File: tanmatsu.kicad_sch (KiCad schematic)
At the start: 41 parts, among them J1 USB device, J10 Expansion I3C, J12 SAO, J2 USB host, J4 Headphone, J5 External Add-On (SAO / PMOD), J6 Internal Add-On, J7 Speaker, J8 Micro_SD_Card, J9 CAMERA, SW3 Boot, U28 USBLC6-2P6, U29 USBLC6-2P6, U30 ESD, U31 ESD, U4 CH334R, Y1 12MHz

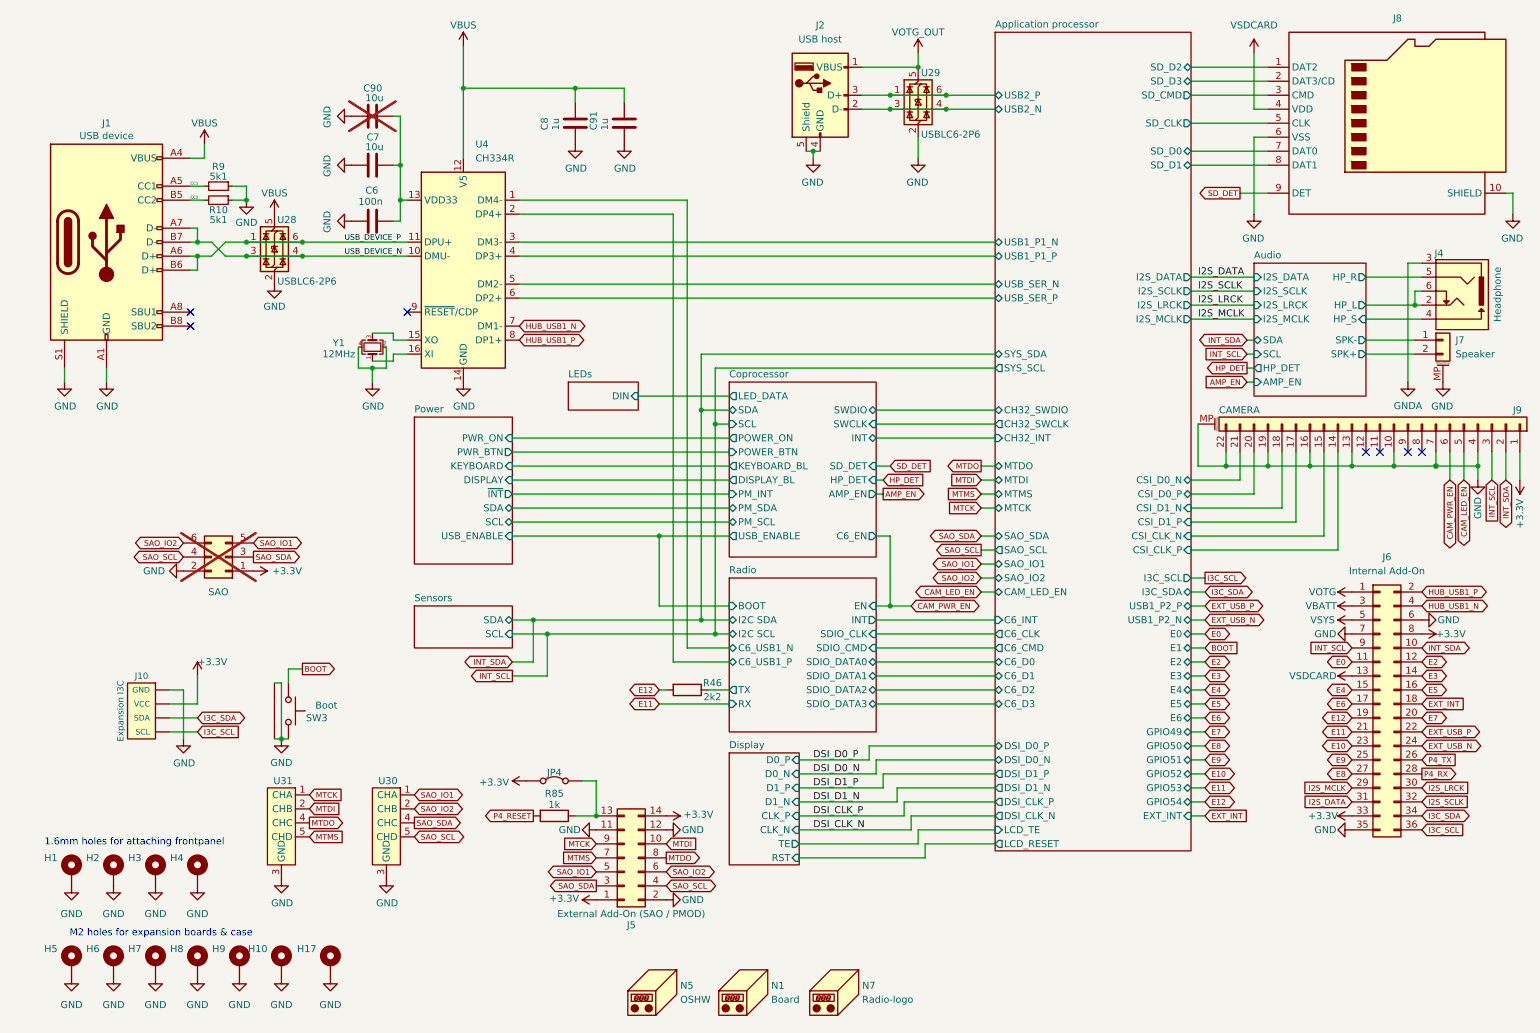
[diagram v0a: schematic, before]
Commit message: Add level shifter for VSDCARD GPIOs, remove USB to serial chip
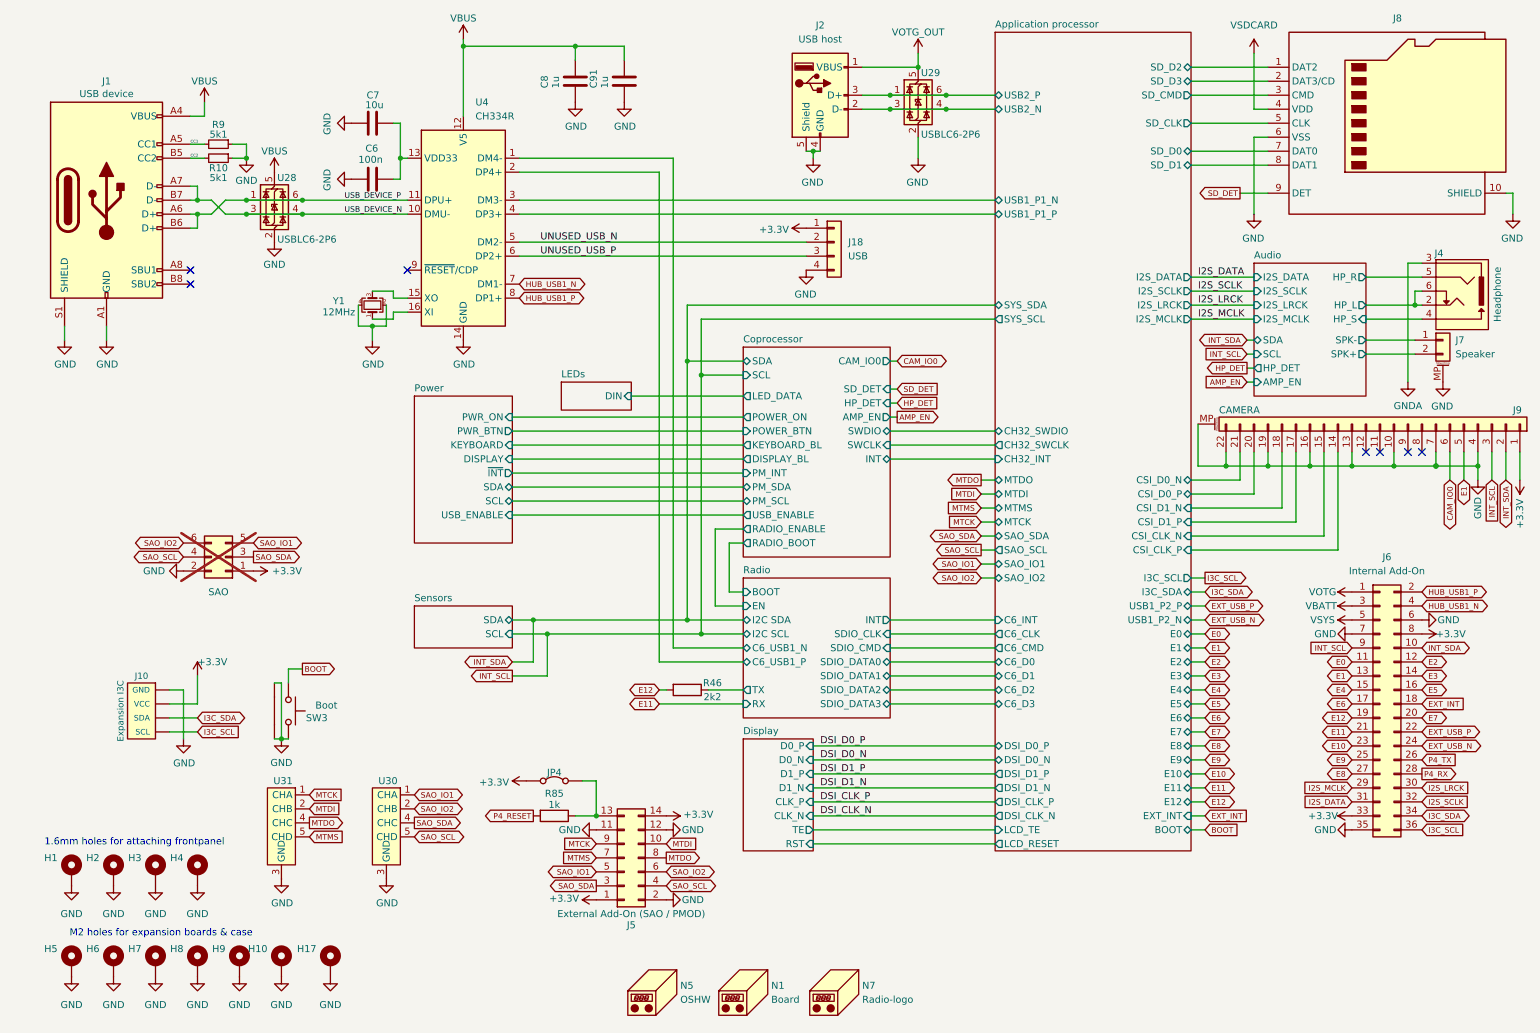
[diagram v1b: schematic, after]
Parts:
- removed C90: 10u, Capacitor_SMD:C_0805_2012Metric, symbol Device:C
- added J18: USB, Connector_PinHeader_2.54mm:PinHeader_1x04_P2.54mm_Vertical_SMD_Pin1Left, symbol Connector_Generic:Conn_01x04
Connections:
- net +3.3V: now also J18.1 (Pin_1)
- net GND: now also J18.4 (Pin_4)
- net VSDCARD: no longer J6.13 (Pin_13)
- net Application processor/USB_SER_N renamed UNUSED_USB_N
- net UNUSED_USB_N: now also J18.2 (Pin_2)
- net Application processor/USB_SER_P renamed UNUSED_USB_P
- net UNUSED_USB_P: now also J18.3 (Pin_3)
- net CAM_LED_EN renamed E1
- net E1: now also J6.13 (Pin_13)
- net CAM_PWR_EN renamed CAM_IO0
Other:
- sheet Application processor ports: added BOOT, E10, E11, E12, E7, E8, E9; removed CAM_LED_EN, GPIO49, GPIO50, GPIO51, GPIO52, GPIO53, GPIO54, USB_SER_N, USB_SER_P
- sheet Coprocessor ports: added CAM_IO0, RADIO_BOOT, RADIO_ENABLE; removed C6_EN
- moved on the sheet: C6, C7, C8, C91, J1, R10, R9, U28, U4, Y1

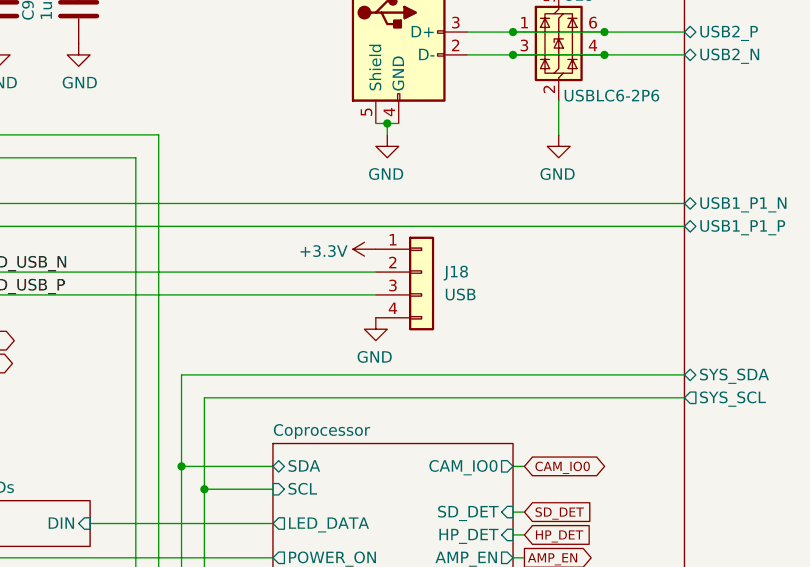
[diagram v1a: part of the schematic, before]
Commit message: Add MCH2022 style battery connector as DNP, use correct footprint for PH style battery connector
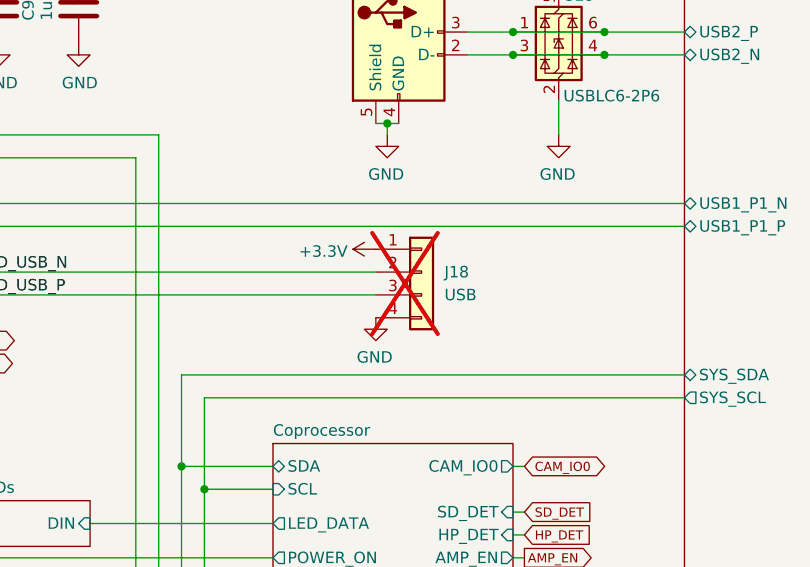
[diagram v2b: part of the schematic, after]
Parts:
- J18: LCSC (none) -> -; now not fitted
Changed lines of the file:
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@@
 		(in_bom yes)
 		(on_board yes)
-		(dnp no)
+		(dnp yes)
 		(fields_autoplaced yes)
 		(property "Reference" "J18"
@@
 			(at 158.75 54.61 0)
 			(effects
+				(font
+					(size 1.27 1.27)
+				)
+				(hide yes)
+			)
+		)
+		(property "LCSC" "-"
+			(at 158.75 54.61 0)
+			(effects

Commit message: Tanmatsu prototype
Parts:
- removed N7: Radio-logo, radio-logo:radio-logo, symbol Mechanical:Housing
- added N3: Nicolai Electronics, library:logo_nicolai, symbol Mechanical:Housing
- J9: renamed from J10; LCSC C160404 -> C7433425
- renumbered C8 to C1, C91 to C2, C7 to C3, C6 to C4, H17 to H11, J2 to J1, J6 to J10, J5 to J11, J8 to J2, J1 to J3, J18 to J4, J4 to J5, J7 to J6, J9 to J7, J12 to J8, JP4 to JP1, N5 to N1, N1 to N2, R9 to R1, R10 to R2, R46 to R3, R85 to R4, SW3 to SW1, U29 to U1, U28 to U2, U4 to U3, U31 to U4, U30 to U5
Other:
- moved on the sheet: N1, N2

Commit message: Preparation for production
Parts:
- J6: LCSC C189700 -> C3029359
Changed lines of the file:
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@@
 	(title_block
 		(title "Tanmatsu")
-		(date "2024-12-30")
-		(rev "0.9")
+		(date "2024-12-31")
+		(rev "1.0")
 		(company "Nicolai Electronics")
 		(comment 1 "Copyright 2024 Paul Honig")
@@
 			)
 		)
-		(property "Datasheet" "https://datasheet.lcsc.com/lcsc/2304140030_MOLEX-532610271_C189700.pdf"
+		(property "Datasheet" "https://www.lcsc.com/product-detail/Wire-To-Board-Connector_XUNPU-WAFER-MX1-25-2PWB_C3029359.html"
 			(at 268.986 73.66 0)
 			(effects
@@
 			)
 		)
-		(property "LCSC" "C189700"
-			(at 269.24 72.39 0)
-			(effects
-				(font
-					(size 1.27 1.27)
-				)
-				(hide yes)
-			)
-		)
-		(property "Check_prices" ""
-			(at 269.24 72.39 0)
-			(effects
-				(font
-					(size 1.27 1.27)
-				)
-				(hide yes)
-			)
-		)
-		(property "Description_1" ""
-			(at 269.24 72.39 0)
-			(effects
-				(font
-					(size 1.27 1.27)
-				)
-				(hide yes)
-			)
-		)
-		(property "Category" ""
+		(property "LCSC" "C3029359"
 			(at 269.24 72.39 0)
 			(effects

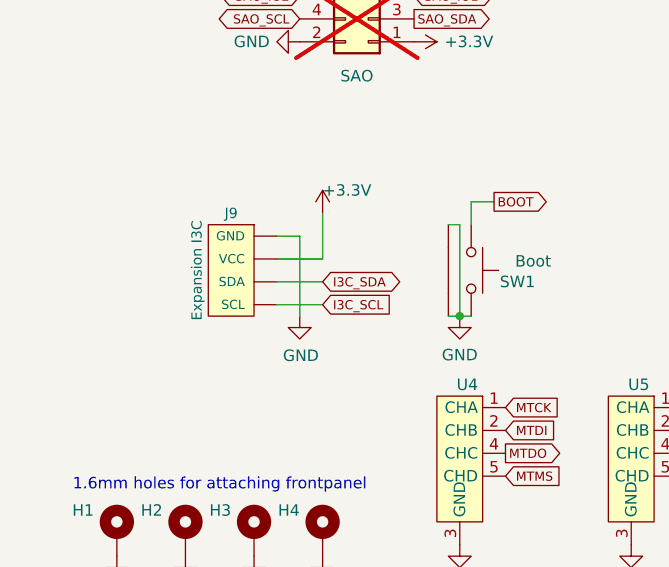
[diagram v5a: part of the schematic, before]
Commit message: Add ESD protection to I3C port, add LCSC ID for SMA connector, small tweaks
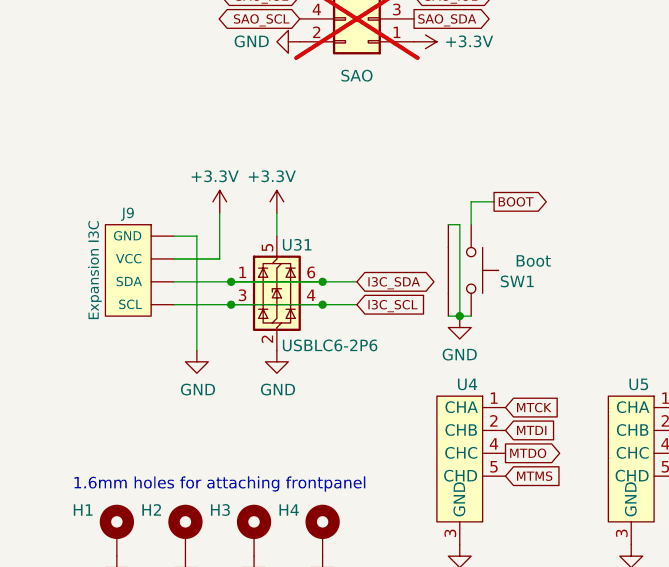
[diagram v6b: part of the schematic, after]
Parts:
- added U31: USBLC6-2P6, Package_TO_SOT_SMD:SOT-666, symbol Power_Protection:USBLC6-2P6
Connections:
- net +3.3V: now also U31.5 (VBUS)
- net GND: now also U31.2 (GND)
- net I3C_SCL: now also U31.3 (I/O2), U31.4 (I/O2)
- net I3C_SDA: now also U31.1 (I/O1), U31.6 (I/O1)
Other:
- moved on the sheet: J9

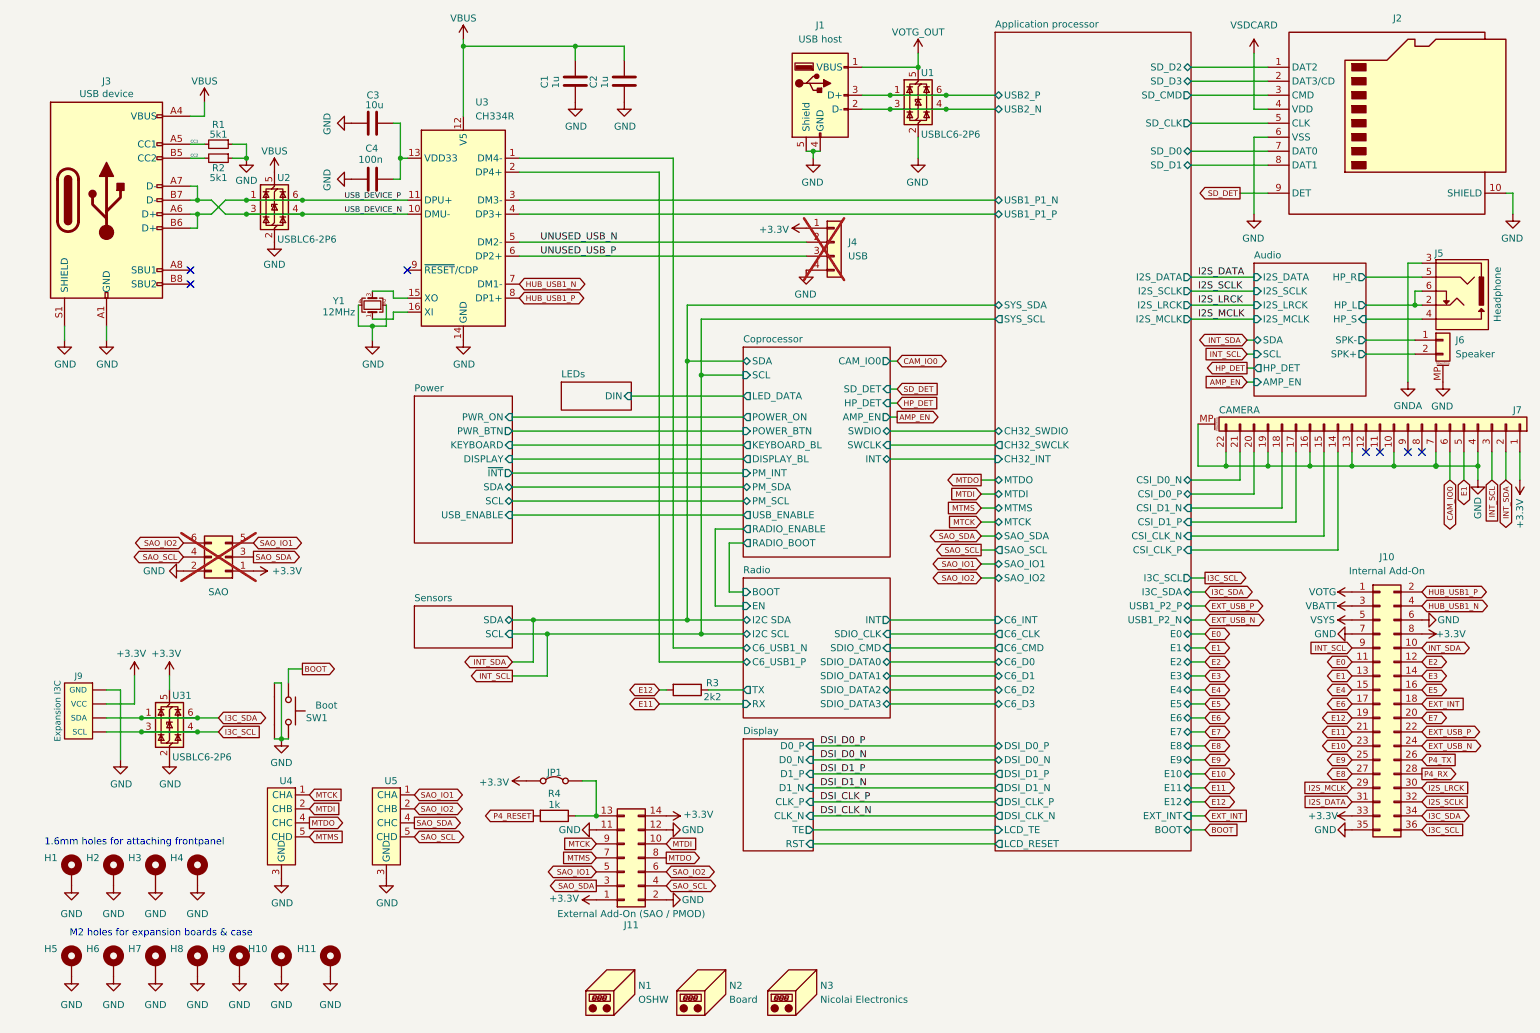
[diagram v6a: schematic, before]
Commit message: ESD protection on 3.3v for CATT connector, new LoRa module, compliance symbols
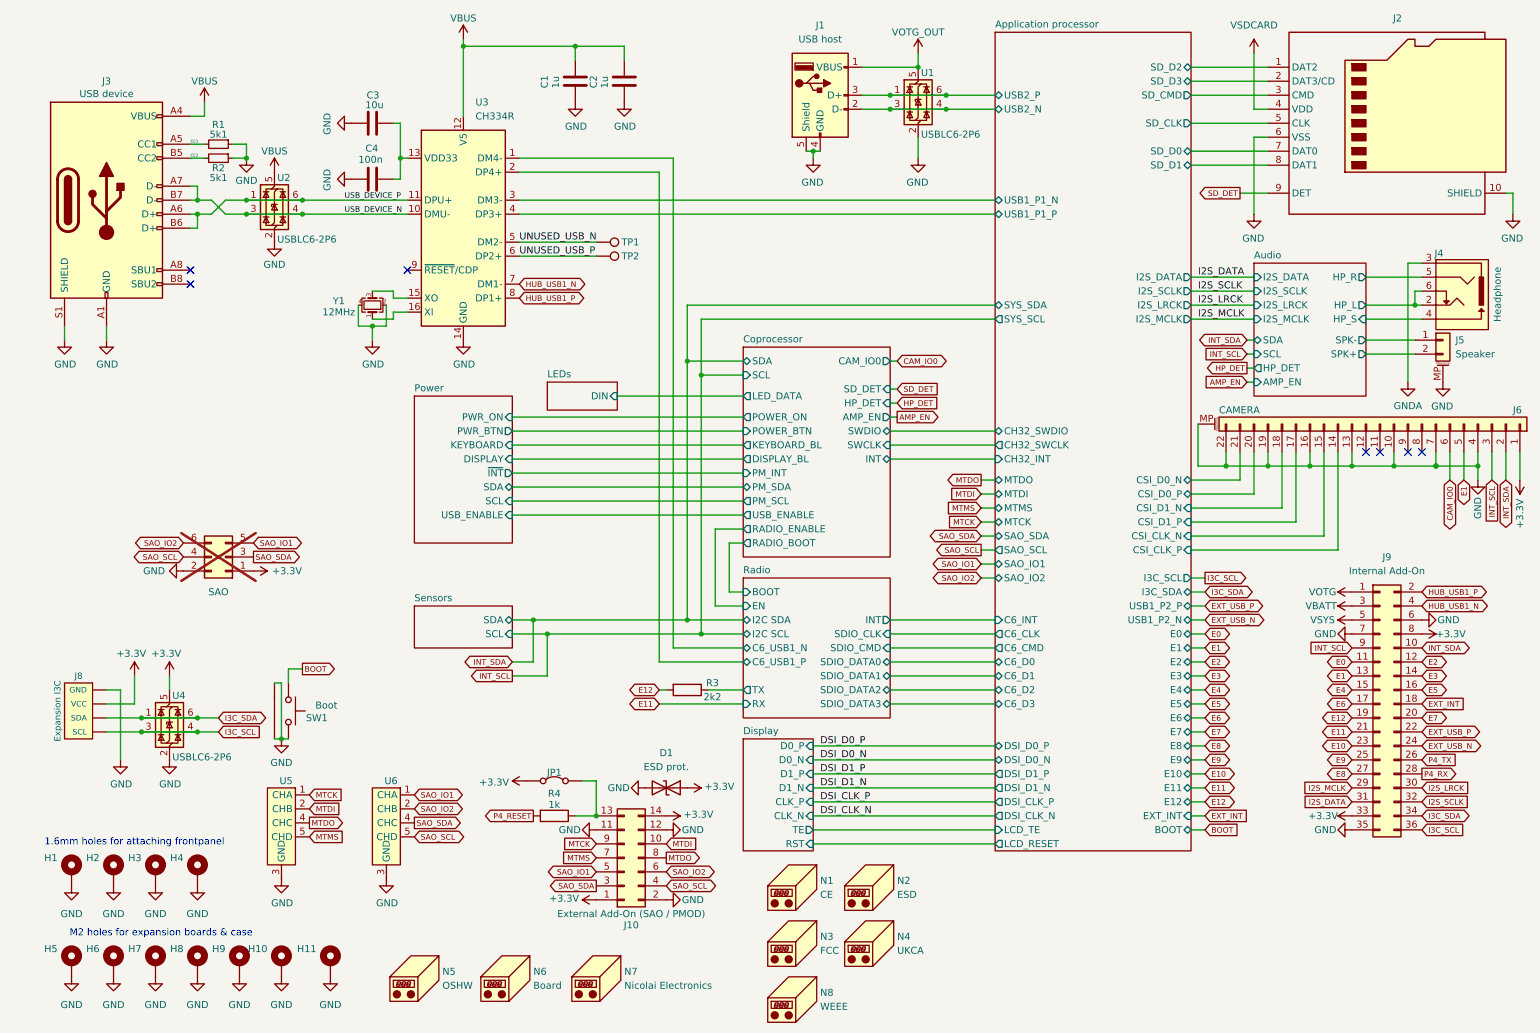
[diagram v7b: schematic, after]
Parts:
- removed J4: USB, Connector_PinHeader_2.54mm:PinHeader_1x04_P2.54mm_Vertical_SMD_Pin1Left, symbol Connector_Generic:Conn_01x04
- added D1: ESD prot., Diode_SMD:D_SOD-323, symbol Device:D_TVS
- added N1: CE, Symbol:CE-Logo_8.5x6mm_SilkScreen, symbol Mechanical:Housing
- added N2: ESD, Symbol:ESD-Logo_6.6x6mm_SilkScreen, symbol Mechanical:Housing
- added N3: FCC, Symbol:FCC-Logo_7.3x6mm_SilkScreen, symbol Mechanical:Housing
- added N4: UKCA, Symbol:UKCA-Logo_6x6mm_SilkScreen, symbol Mechanical:Housing
- added N8: WEEE, Symbol:WEEE-Logo_4.2x6mm_SilkScreen, symbol Mechanical:Housing
- added TP1: D-, TestPoint:TestPoint_Pad_D1.0mm, symbol Connector:TestPoint
- added TP2: D+, TestPoint:TestPoint_Pad_D1.0mm, symbol Connector:TestPoint
- renumbered J11 to J10, J5 to J4, J6 to J5, J7 to J6, J8 to J7, J9 to J8, J10 to J9, N1 to N5, N2 to N6, N3 to N7, U31 to U4, U4 to U5, U5 to U6
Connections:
- net +3.3V: now also D1.1 (A1)
- net GND: now also D1.2 (A2)
- net UNUSED_USB_N: now also TP1.1
- net UNUSED_USB_P: now also TP2.1
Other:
- moved on the sheet: N5, N6, N7
